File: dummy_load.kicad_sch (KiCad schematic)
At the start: 12 parts, among them Q1 IRFZ44N, U1 TL082, U2 TL082

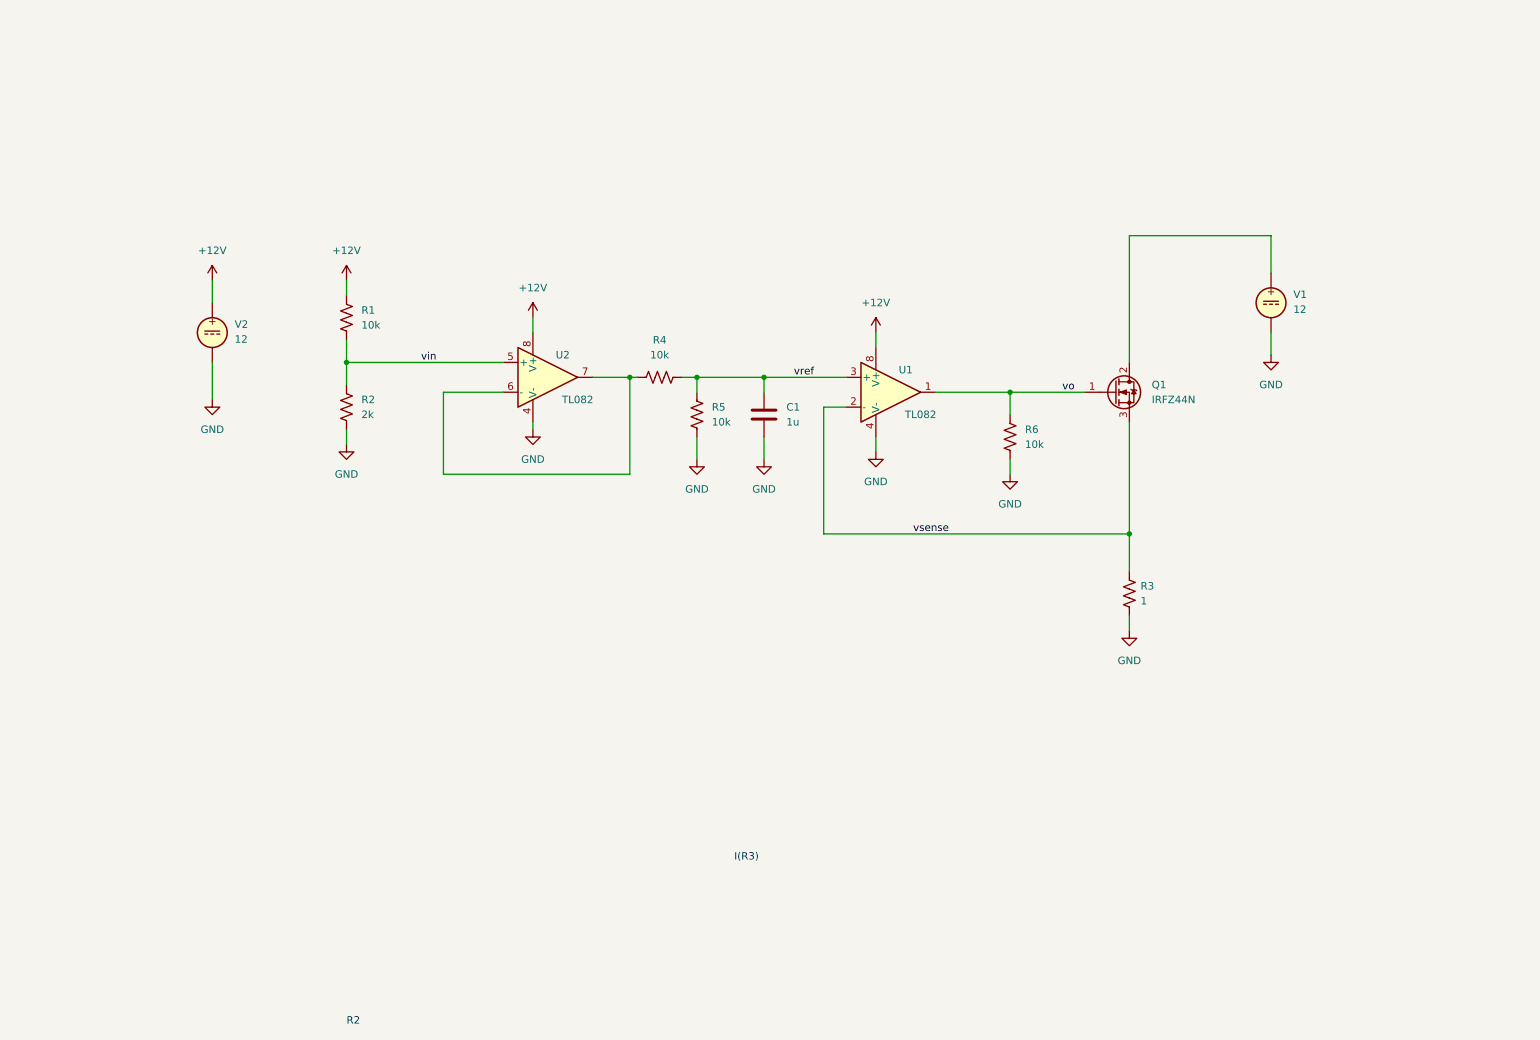
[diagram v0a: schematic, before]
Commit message: version con LM358 (SIMULACION)
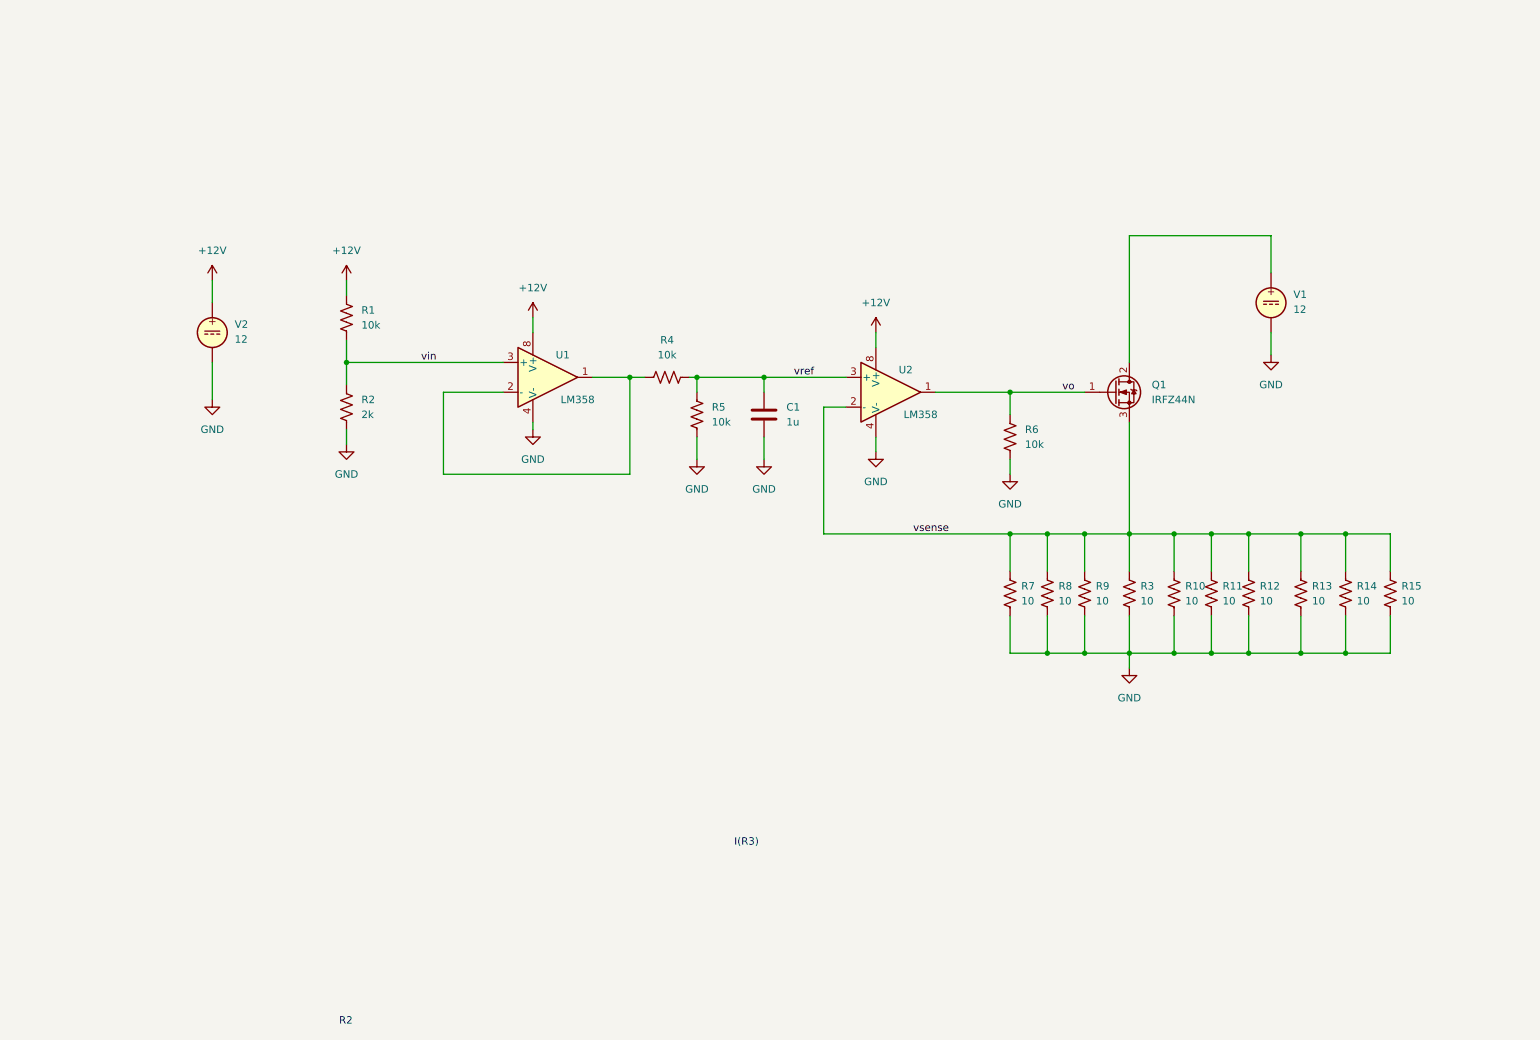
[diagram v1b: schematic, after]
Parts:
- added R10, R11, R12, R13, R14, R15, R7, R8, R9: 10, Resistor_THT:R_Axial_DIN0414_L11.9mm_D4.5mm_P15.24mm_Horizontal, symbol Device:R_US
- Q1: footprint (none) -> Package_TO_SOT_THT:TO-220-3_Horizontal_TabDown
- R1, R2, R4, R5, R6: footprint (none) -> Resistor_THT:R_Axial_DIN0207_L6.3mm_D2.5mm_P10.16mm_Horizontal
- R3: value 1 -> 10; footprint (none) -> Resistor_THT:R_Axial_DIN0414_L11.9mm_D4.5mm_P15.24mm_Horizontal
- U1, U2: value TL082 -> LM358
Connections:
- net GND: now also R10.2, R11.2, R12.2, R13.2, R14.2, R15.2, R7.2, R8.2, R9.2
- net vin: now also U1.3 (+); no longer U2.5 (+)
- net vo: now also U2.1; no longer U1.1
- net vref: now also U2.3 (+); no longer U1.3 (+)
- net vsense: now also U2.2 (-), R10.1, R11.1, R12.1, R13.1, R14.1, R15.1, R7.1, R8.1, R9.1; no longer U1.2 (-)
- new net: R4.2, U1.1, U1.2 (-)
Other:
- moved on the sheet: R4

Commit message: Completada la version 1
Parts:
- removed R1: 10k, Resistor_THT:R_Axial_DIN0207_L6.3mm_D2.5mm_P10.16mm_Horizontal, symbol Device:R_US
- removed R2: 2k, Resistor_THT:R_Axial_DIN0207_L6.3mm_D2.5mm_P10.16mm_Horizontal, symbol Device:R_US
- removed U1, U2: LM358, symbol Simulation_SPICE:OPAMP
- removed V1, V2: 12, symbol Simulation_SPICE:VDC
- added C2: 100nF, Capacitor_THT:C_Disc_D5.0mm_W2.5mm_P2.50mm, symbol Device:C
- added H1, H2, H3, H4: MountingHole, MountingHole:MountingHole_3.2mm_M3_Pad_Via, symbol Mechanical:MountingHole
- added HS1: Heatsink, MR-footprint:disipador_VGA, symbol Mechanical:Heatsink
- added J1: Conn_01x02, Connector_BarrelJack:BarrelJack_Horizontal, symbol Connector_Generic:Conn_01x02
- added J2: Conn_01x02, TerminalBlock_Phoenix:TerminalBlock_Phoenix_MKDS-1,5-2-5.08_1x02_P5.08mm_Horizontal, symbol Connector_Generic:Conn_01x02
- added J3: PH_B2B-PH-K, Connector_JST:JST_PH_B2B-PH-K_1x02_P2.00mm_Vertical, symbol Connector_Generic:Conn_01x02
- added RV1: 5k, Potentiometer_THT:Potentiometer_Alps_RK09Y11_Single_Horizontal, symbol Device:R_Potentiometer_US
- added U1: LM358, symbol Amplifier_Operational:LM358
- C1: value 1u -> 1uF; footprint (none) -> Capacitor_THT:C_Disc_D5.0mm_W2.5mm_P5.00mm
- Q1: footprint Package_TO_SOT_THT:TO-220-3_Horizontal_TabDown -> Package_TO_SOT_THT:TO-220-3_Horizontal_TabUp
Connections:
- net +12V: now also C2.1, J1.2 (Pin_2), J3.2 (Pin_2), RV1.1, U1.8 (V+)
- net GND: now also C2.2, J1.1 (Pin_1), J2.2 (Pin_2), J3.1 (Pin_1), RV1.3, U1.4 (V-)
- net vin: now also RV1.2, U1.5 (+)
- net vo: now also U1.1
- net vref: now also U1.3 (+)
- net vsense: now also U1.2 (-)
- net at R4.2: now also U1.6 (-), U1.7
- net at Q1.2 (D): now also J2.1 (Pin_1)

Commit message: creando archivos de fabricación
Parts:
- U1: footprint (none) -> Package_DIP:DIP-8_W7.62mm_Socket
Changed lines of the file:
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@@
 			)
 		)
-		(property "Footprint" ""
+		(property "Footprint" "Package_DIP:DIP-8_W7.62mm_Socket"
 			(at 43.18 80.01 0)
 			(effects
@@
 		)
 		(property "Description" ""
+			(at 43.18 80.01 0)
+			(effects
+				(font
+					(size 1.27 1.27)
+				)
+				(hide yes)
+			)
+		)
+		(property "LCSC Part" ""
+			(at 43.18 80.01 0)
+			(effects
+				(font
+					(size 1.27 1.27)
+				)
+				(hide yes)
+			)
+		)
+		(property "Mfr. Part" ""
+			(at 43.18 80.01 0)
+			(effects
+				(font
+					(size 1.27 1.27)
+				)
+				(hide yes)
+			)
+		)
+		(property "Manufacturer" ""
+			(at 43.18 80.01 0)
+			(effects
+				(font
+					(size 1.27 1.27)
+				)
+				(hide yes)
+			)
+		)
+		(property "Price" ""
 			(at 43.18 80.01 0)
 			(effects
@@
 			)
 		)
-		(property "Footprint" ""
+		(property "Footprint" "Package_DIP:DIP-8_W7.62mm_Socket"
 			(at 116.84 86.36 0)
 			(effects
@@
 			(at 116.84 86.36 0)
 			(effects
+				(font
+					(size 1.27 1.27)
+				)
+				(hide yes)
+			)
+		)
+		(property "LCSC Part" ""
+			(at 116.84 86.36 0)
+			(effects
+				(font
+					(size 1.27 1.27)
+				)
+				(hide yes)
+			)
+		)
+		(property "Mfr. Part" ""
+			(at 116.84 86.36 0)
+			(effects
+				(font
+					(size 1.27 1.27)
+				)
+				(hide yes)
+			)
+		)
+		(property "Manufacturer" ""
+			(at 116.84 86.36 0)
+			(effects
+				(font
+					(size 1.27 1.27)
+				)
+				(hide yes)
+			)
+		)
+		(property "Price" ""
+			(at 116.84 86.36 0)
+			(effects

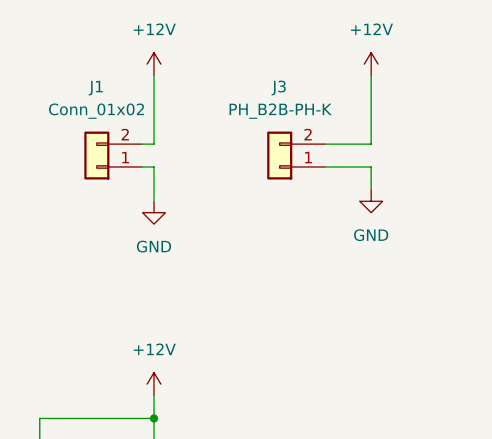
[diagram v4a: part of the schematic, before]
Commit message: corrigiendo el conector jack-DC invertido
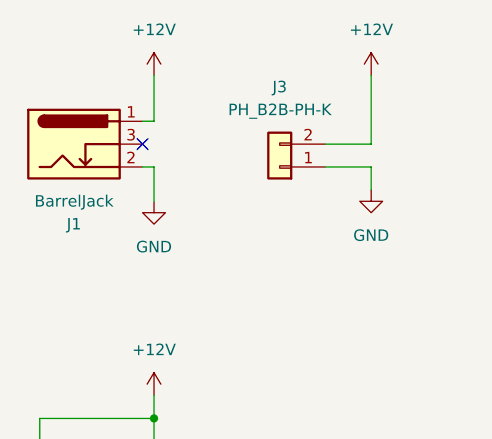
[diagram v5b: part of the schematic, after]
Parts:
- J1: value Conn_01x02 -> BarrelJack; symbol Connector_Generic:Conn_01x02 -> Connector:Barrel_Jack_Switch
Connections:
- net +12V: now also J1.1; no longer J1.2 (Pin_2)
- net GND: now also J1.2; no longer J1.1 (Pin_1)
- no-connect marks 0 -> 1
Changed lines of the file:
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@@
 		(title "Carga Electronica ")
 		(date "2023-11-26")
-		(rev "v1.0.1")
+		(rev "v1.1.0")
 	)
 	(junction
@@
 		(color 0 0 0 0)
 	)
+	(no_connect
+		(at 39.37 38.1)
+	)
 	(wire
 		(pts
@@
 	(wire
 		(pts
+			(xy 40.64 35.56) (xy 40.64 30.48)
+		)
+		(stroke
+			(width 0)
+			(type default)
+		)
+	)
+	(wire
+		(pts
 			(xy 215.9 119.38) (xy 215.9 113.03)
 		)
@@
 	(wire
 		(pts
-			(xy 39.37 38.1) (xy 40.64 38.1)
-		)
-		(stroke
-			(width 0)
-			(type default)
-		)
-	)
-	(wire
-		(pts
 			(xy 59.69 40.64) (xy 64.77 40.64)
 		)
@@
 	(wire
 		(pts
-			(xy 40.64 30.48) (xy 40.64 38.1)
-		)
-		(stroke
-			(width 0)
-			(type default)
-		)
-	)
-	(wire
-		(pts
 			(xy 240.03 62.23) (xy 240.03 72.39)
 		)
@@
 	(wire
 		(pts
+			(xy 39.37 35.56) (xy 40.64 35.56)
+		)
+		(stroke
+			(width 0)
+			(type default)
+		)
+	)
+	(wire
+		(pts
 			(xy 245.11 133.35) (xy 236.22 133.35)
 		)
@@
 	)
 	(symbol
-		(lib_id "Connector_Generic:Conn_01x02")
-		(at 34.29 40.64 180)
+		(lib_id "Connector:Barrel_Jack_Switch")
+		(at 31.75 38.1 0)
 		(unit 1)
 		(exclude_from_sim no)
@@
 		(on_board yes)
 		(dnp no)
-		(fields_autoplaced yes)
 		(property "Reference" "J1"
-			(at 34.29 31.75 0)
+			(at 31.75 46.99 0)
 			(effects
 				(font
@@
 			)
 		)
-		(property "Value" "Conn_01x02"
-			(at 34.29 34.29 0)
+		(property "Value" "BarrelJack"
+			(at 31.75 44.45 0)
 			(effects
 				(font
@@
 		)
 		(property "Footprint" "Connector_BarrelJack:BarrelJack_Horizontal"
-			(at 34.29 40.64 0)
+			(at 33.02 39.116 0)
 			(effects
 				(font
@@
 		)
 		(property "Datasheet" "~"
-			(at 34.29 40.64 0)
+			(at 33.02 39.116 0)
 			(effects
 				(font
@@
 			)
 		)
-		(property "Description" ""
-			(at 34.29 40.64 0)
+		(property "Description" "DC Barrel Jack with an internal switch"
+			(at 31.75 38.1 0)
 			(effects
 				(font
@@
 		)
 		(property "LCSC Part" ""
-			(at 34.29 40.64 0)
+			(at 31.75 38.1 0)
 			(effects
 				(font
@@
 		)
 		(property "Mfr. Part" ""
-			(at 34.29 40.64 0)
+			(at 31.75 38.1 0)
 			(effects
 				(font
@@
 		)
 		(property "Manufacturer" ""
-			(at 34.29 40.64 0)
+			(at 31.75 38.1 0)
 			(effects
 				(font
@@
 		)
 		(property "Price" ""
-			(at 34.29 40.64 0)
+			(at 31.75 38.1 0)
 			(effects
 				(font
@@
 		(pin "1"
 		)
+		(pin "3"
+		)
 		(instances
